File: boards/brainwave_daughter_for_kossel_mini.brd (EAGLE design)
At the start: 79 x 70 mm, 18 parts, among them U6 7805

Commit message: finished first draft of extruder and daughter boards
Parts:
- removed C22, C23: 1uF, rcl:C0603
- removed C28, C29: 47uF, rcl:153CLV-0605
- removed U6: 7805, shinythings:SOT89
- added BED_LED_HEDR: (no value), con-lstb:MA03-1
- added D0_LMT_HEDR, D1_LMT_HEDR, D2_LMT_HEDR: (no value), jumper:JP1
- added EXTRUDER_HEDR: (no value), con-lstb:MA05-2
- added EXTRUDER_MOTOR_HEDR: (no value), con-lstb:MA04-1
- added LED_HEDR: (no value), con-lstb:MA04-2
- added PLUG: (no value), con-wago-500:W237-102
- renumbered E to EXTRUDER_SOCKET
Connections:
- new net N$1: D0_LMT_HEDR.1, X_MIN.1
- new net N$10: EXTRUDER_MOTOR_HEDR.3, EXTRUDER_SOCKET.5
- new net N$11: EXTRUDER_MOTOR_HEDR.4, EXTRUDER_SOCKET.7
- new net N$2: D1_LMT_HEDR.1, Y_MIN.1
- new net N$3: D2_LMT_HEDR.1, Z_MIN.1
- new net N$4: D2_LMT_HEDR.2, Z_MIN.2
- new net N$5: D1_LMT_HEDR.2, Y_MIN.2
- new net N$6: D0_LMT_HEDR.2, X_MIN.2
- new net N$7: EXTRUDER_HEDR.1, FAN.1
- new net N$8: EXTRUDER_MOTOR_HEDR.1, EXTRUDER_SOCKET.1
- new net N$9: EXTRUDER_MOTOR_HEDR.2, EXTRUDER_SOCKET.3
- net +12V: now also EXTRUDER_HEDR.10, EXTRUDER_HEDR.8, PLUG.2; no longer C22.1, C29.+, EXTRUDER_SOCKET.8, U6.3
- net E_POWER: now also EXTRUDER_HEDR.2, EXTRUDER_HEDR.4
- net E_TEMP: now also EXTRUDER_HEDR.9
- net GND: now also BED_LED_HEDR.3, EXTRUDER_HEDR.5, EXTRUDER_HEDR.6, LED_HEDR.2, LED_HEDR.4, LED_HEDR.6, LED_HEDR.8, PLUG.1; no longer C22.2, C23.2, C28.-, C29.-, U6.2, U6.2@1
- net MISO: now also EXTRUDER_HEDR.7
- net MOSI: now also BED_LED_HEDR.1
- net VCC: now also BED_LED_HEDR.2, EXTRUDER_HEDR.3, LED_HEDR.1, LED_HEDR.3, LED_HEDR.5, LED_HEDR.7; no longer C23.1, C28.+, U6.1
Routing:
- net GND: track 0.00 -> 174.3 mm
- net VCC: track 0.59 -> 73.2 mm
- net +12V: track 0.00 -> 69.6 mm
- net N$7: track 0.00 -> 66.5 mm
- net MOSI: track 0.00 -> 64.5 mm, vias 0 -> 1
- net E_TEMP: track 0.00 -> 52.5 mm
- net N$3: track 0.00 -> 49.1 mm
- net MISO: track 0.00 -> 46.5 mm, vias 0 -> 1
- net N$4: track 0.00 -> 44.3 mm
- net E_POWER: track 0.00 -> 40.1 mm
- net N$2: track 0.00 -> 37.4 mm
- net N$5: track 0.00 -> 32.6 mm
- net N$11: track 0.00 -> 32.1 mm
- net N$10: track 0.00 -> 26.0 mm
- net N$1: track 0.00 -> 26.0 mm
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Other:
- board size 79 x 70 mm -> 79 x 72 mm

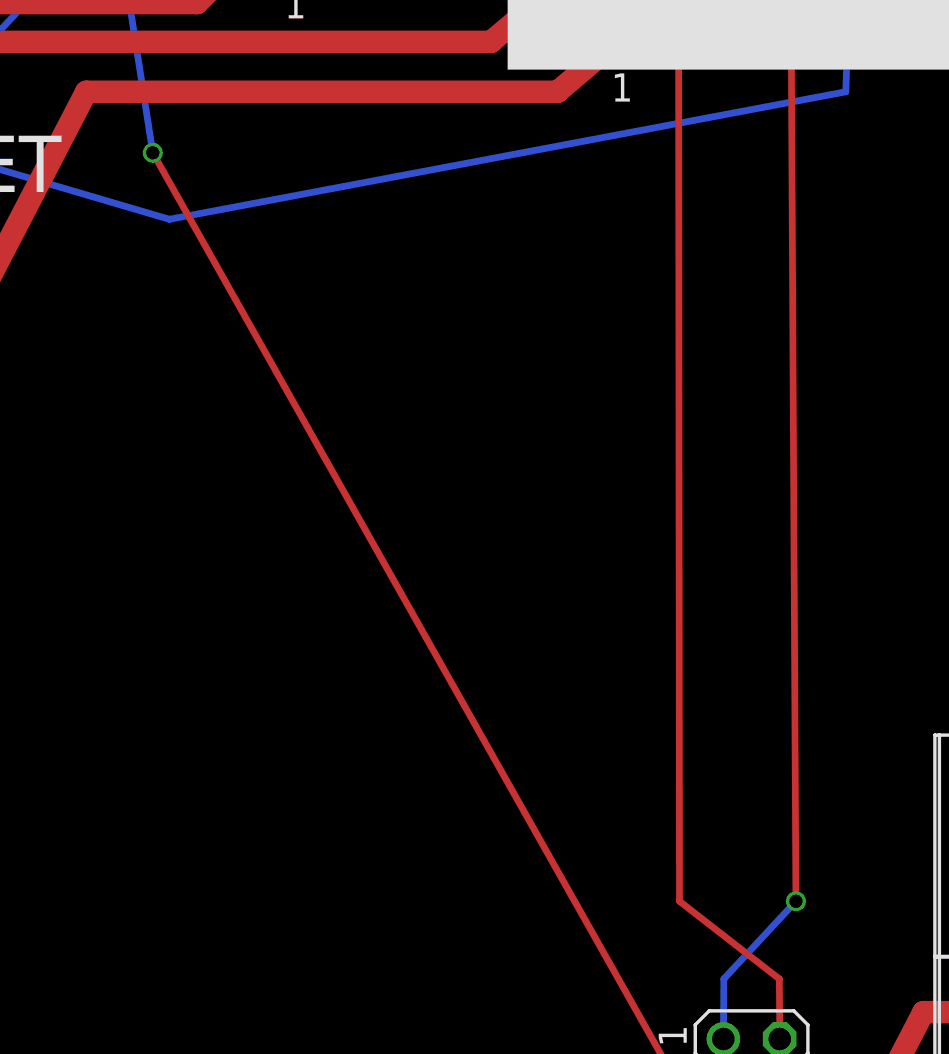
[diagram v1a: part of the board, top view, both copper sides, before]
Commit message: made vias beefier for hand soldering
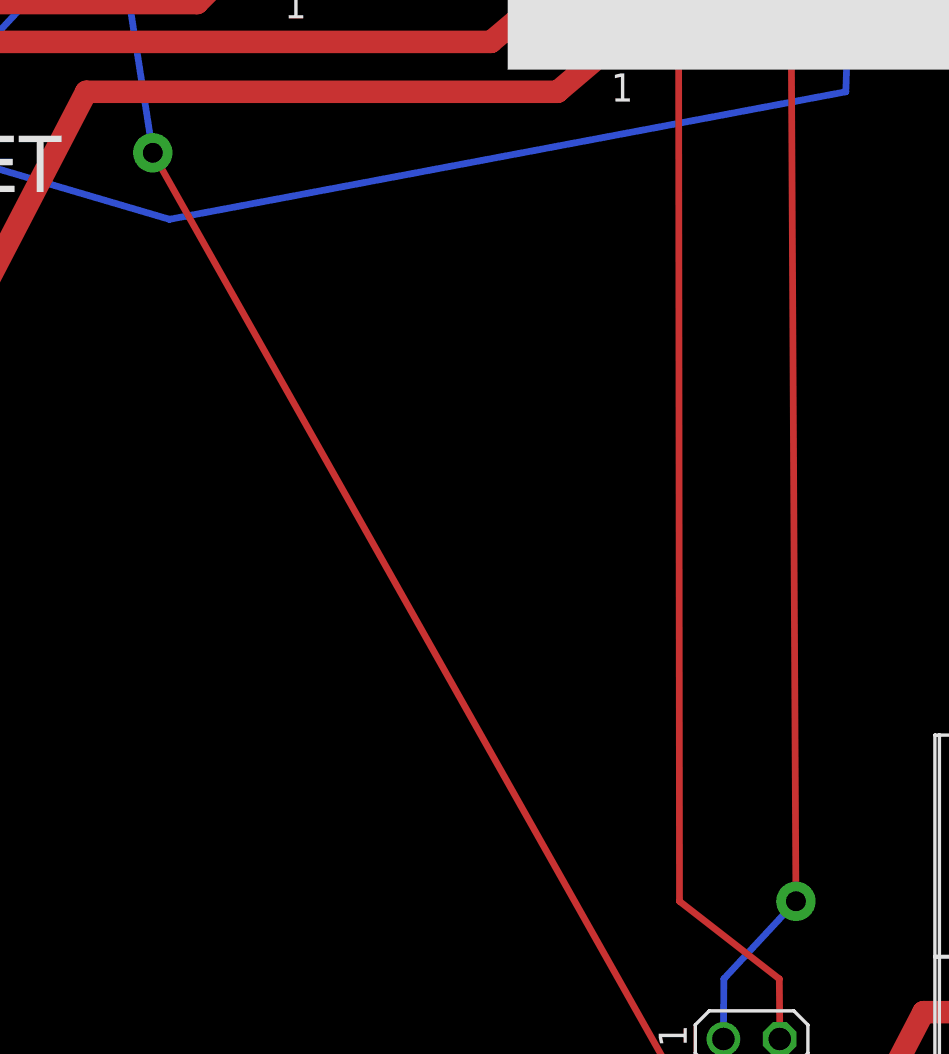
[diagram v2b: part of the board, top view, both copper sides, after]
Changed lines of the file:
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@@
 <contactref element="BED_LED_HEDR" pad="1"/>
 <wire x1="29.21" y1="68.75" x2="31" y2="57.25" width="0.3048" layer="16"/>
-<via x="31" y="57.25" extent="1-16" drill="0.6"/>
+<via x="31" y="57.25" extent="1-16" drill="0.9" diameter="1.778"/>
 <wire x1="31" y1="57.25" x2="54.25" y2="16" width="0.3048" layer="1"/>
 <wire x1="54.25" y1="16" x2="58" y2="16" width="0.3048" layer="1"/>
@@
 <wire x1="60" y1="23.5" x2="56.75" y2="20" width="0.3048" layer="16"/>
 <wire x1="56.75" y1="20" x2="56.73" y2="17.29" width="0.3048" layer="16"/>
-<via x="60" y="23.5" extent="1-16" drill="0.6"/>
+<via x="60" y="23.5" extent="1-16" drill="0.9" diameter="1.778"/>
 <wire x1="60" y1="23.5" x2="59.79" y2="62.48" width="0.3048" layer="1"/>
 </signal>

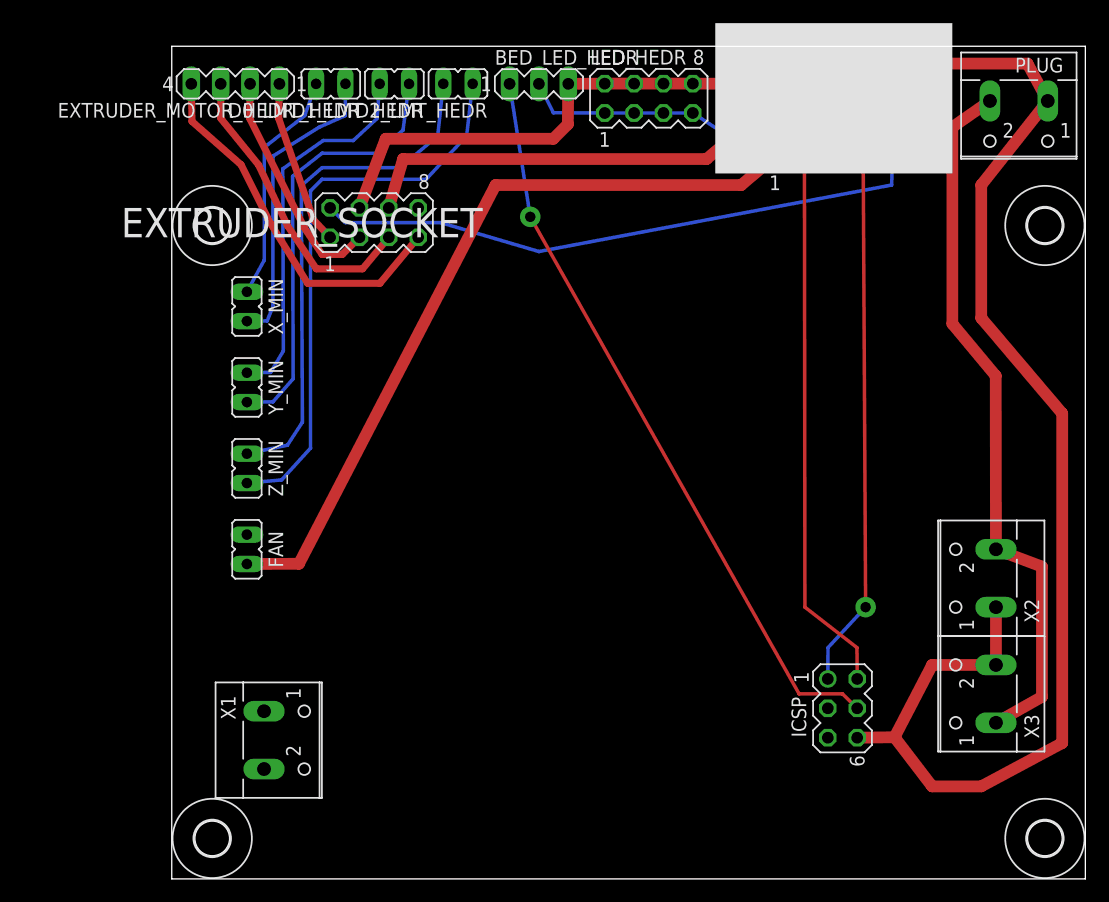
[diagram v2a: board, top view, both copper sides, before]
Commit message: replaced 2x5 header with 2x4 header
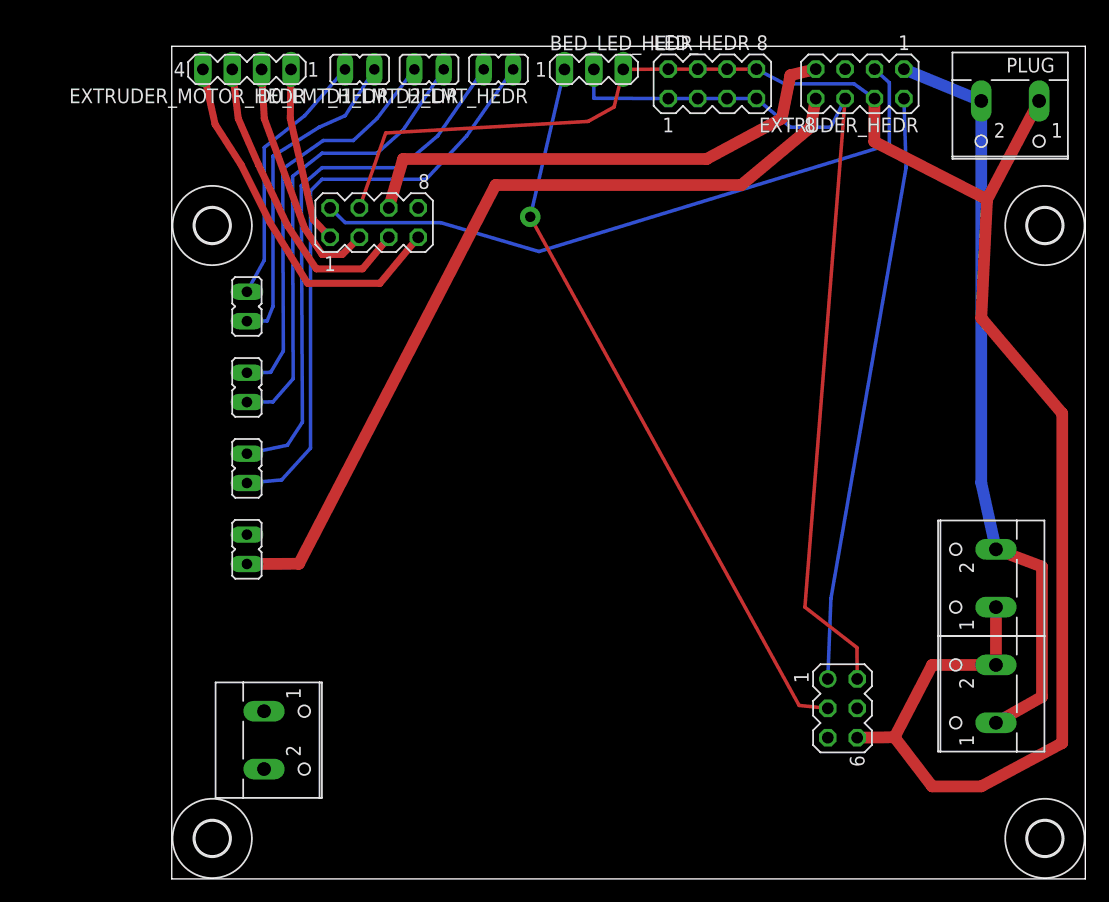
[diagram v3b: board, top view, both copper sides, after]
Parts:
- EXTRUDER_HEDR: device con-lstb:MA05-2 -> con-lstb:MA04-2
- moved LED_HEDR 5.64 mm to (46.8, 68.8)
- moved EXTRUDER_HEDR 5.48 mm to (59.5, 68.8), turned to 180 degrees
- moved BED_LED_HEDR 4.91 mm to (36.5, 70.0)
- moved D2_LMT_HEDR 3.72 mm to (28.2, 70.0)
- moved D1_LMT_HEDR 3.25 mm to (22.2, 70.0)
- moved D0_LMT_HEDR 2.80 mm to (16.2, 70.0)
- moved EXTRUDER_MOTOR_HEDR 1.60 mm to (6.50, 70.0)
- moved PLUG 0.75 mm to (72.5, 66.0)
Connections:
- removed net MOSI: BED_LED_HEDR.1, ICSP.4
- net +12V: now also EXTRUDER_HEDR.1; no longer EXTRUDER_HEDR.10, EXTRUDER_HEDR.8
- net E_POWER: now also EXTRUDER_HEDR.7; no longer EXTRUDER_HEDR.2, EXTRUDER_HEDR.4
- net E_TEMP: now also EXTRUDER_HEDR.3; no longer EXTRUDER_HEDR.9
- net GND: now also EXTRUDER_HEDR.4; no longer EXTRUDER_HEDR.5, EXTRUDER_HEDR.6
- net MISO: now also EXTRUDER_HEDR.2; no longer EXTRUDER_HEDR.7
- net N$7: now also EXTRUDER_HEDR.8; no longer EXTRUDER_HEDR.1
- net SCK: now also BED_LED_HEDR.1
- net VCC: now also EXTRUDER_HEDR.6; no longer EXTRUDER_HEDR.3
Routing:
- net MOSI: track 64.5 -> 0.00 mm, vias 1 -> 0
- net SCK: track 0.00 -> 63.8 mm, vias 0 -> 1
- net GND: track 174.3 -> 165.0 mm
- net N$7: track 66.5 -> 73.0 mm
- net VCC: track 73.2 -> 79.2 mm
- net E_TEMP: track 52.5 -> 57.7 mm
- net MISO: track 46.5 -> 50.8 mm, vias 1 -> 0
- net E_POWER: track 40.1 -> 44.1 mm
- net +12V: track 69.6 -> 66.2 mm
- net N$3: track 49.1 -> 51.5 mm
- net N$4: track 44.3 -> 46.8 mm
- net N$6: track 20.2 -> 22.6 mm
- net N$5: track 32.6 -> 35.0 mm
- net N$2: track 37.4 -> 39.7 mm
- net N$1: track 26.0 -> 28.0 mm
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
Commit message: put fan on separate 12V supply line
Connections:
- net +12V: now also EXTRUDER_HEDR.5
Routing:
- net +12V: track 66.2 -> 72.6 mm
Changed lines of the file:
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@@
 <wire x1="70" y1="67.27" x2="70" y2="34.25" width="1.016" layer="16"/>
 <wire x1="70" y1="34.25" x2="71.27" y2="28.5" width="1.016" layer="16"/>
+<contactref element="EXTRUDER_HEDR" pad="5"/>
+<wire x1="63.31" y1="70.02" x2="62" y2="71.5" width="0.4064" layer="16"/>
+<wire x1="62" y1="71.5" x2="59.75" y2="71.5" width="0.4064" layer="16"/>
+<wire x1="59.75" y1="71.5" x2="58.23" y2="70.02" width="0.4064" layer="16"/>
 </signal>
 <signal name="SCK">
